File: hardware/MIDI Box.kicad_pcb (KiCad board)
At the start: 2 copper layers, 39.1 x 76.5 mm, 33 parts, among them J1 Conn_01x02_Pin, J2 Conn_01x02_Pin, J3 Conn_01x20_Socket, J4 Conn_01x20_Socket, J7 Conn_01x012_Pin, U1 6N138, U2 6N138, U3 40106

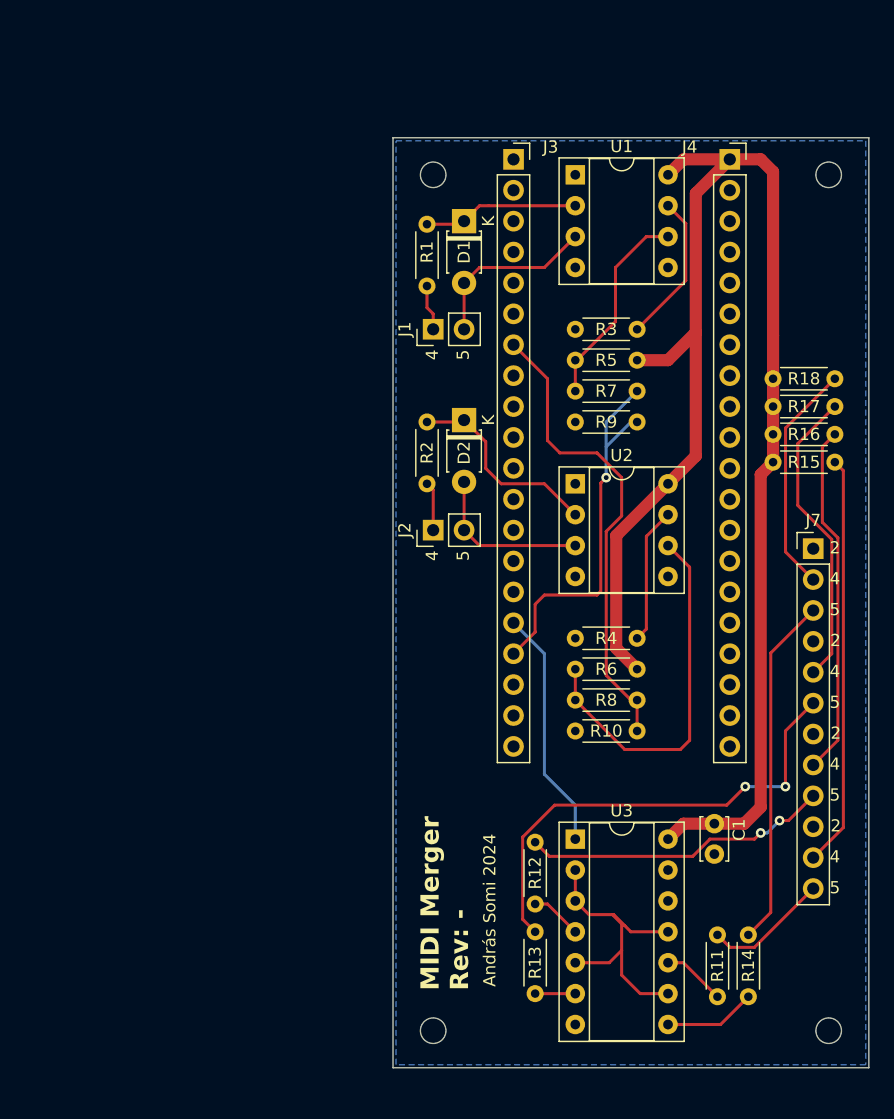
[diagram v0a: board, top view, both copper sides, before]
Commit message: v2.0 board with TRS sockets
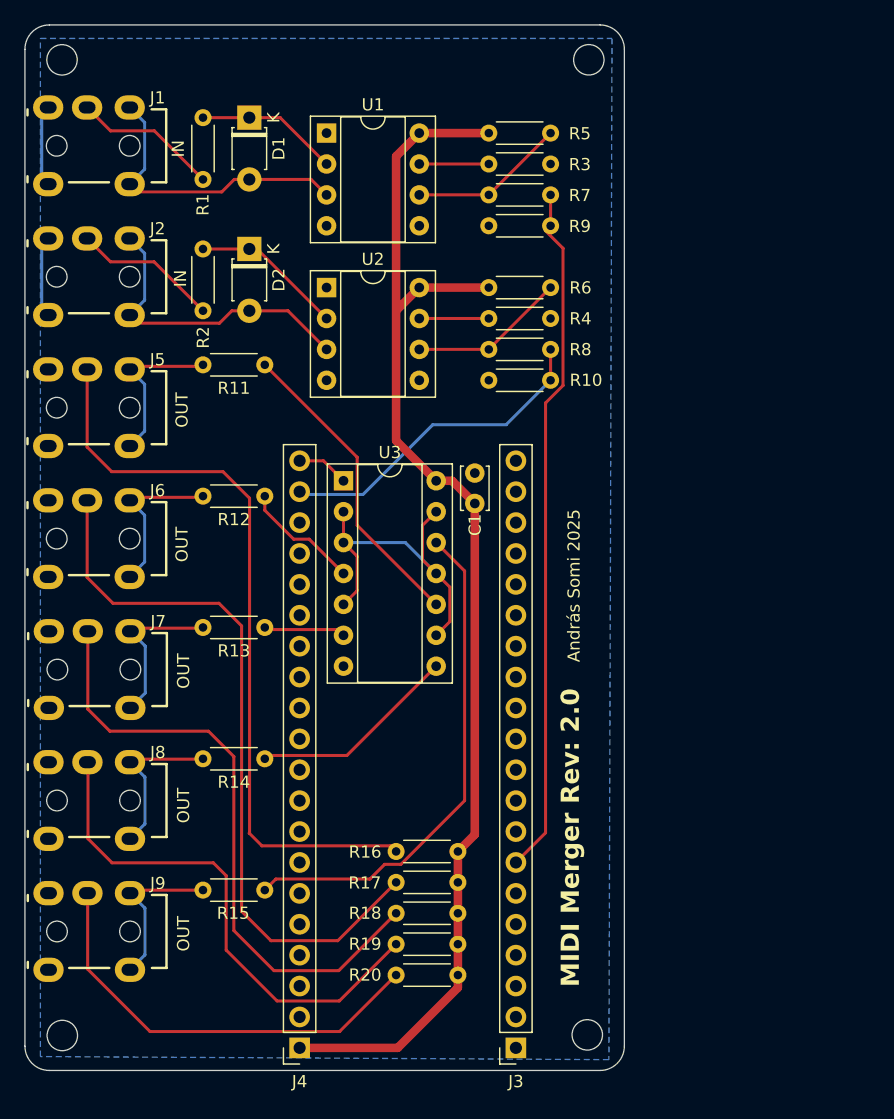
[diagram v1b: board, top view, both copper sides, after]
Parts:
- removed REF** (x4): MountingHole_2.1mm, MountingHole:MountingHole_2.1mm
- added J5: MIDI_OUT_1, own_components:Audio Jack PJ-3136-B, F.Cu at (111.8, 82.9)
- added J6: MIDI_OUT_2, own_components:Audio Jack PJ-3136-B, F.Cu at (111.8, 93.7)
- added J8: MIDI_OUT_4, own_components:Audio Jack PJ-3136-B, F.Cu at (111.9, 115.2)
- added J9: MIDI_OUT_5, own_components:Audio Jack PJ-3136-B, F.Cu at (111.9, 126.0)
- added R19: 220, Resistor_THT:R_Axial_DIN0204_L3.6mm_D1.6mm_P5.08mm_Horizontal, F.Cu at (147.3, 127.0)
- added R20: 220, Resistor_THT:R_Axial_DIN0204_L3.6mm_D1.6mm_P5.08mm_Horizontal, F.Cu at (147.3, 129.5)
- J1: value Conn_01x02_Pin -> MIDI_IN_1; footprint Connector_PinHeader_2.54mm:PinHeader_1x02_P2.54mm_Vertical -> own_components:Audio Jack PJ-3136-B
- J2: value Conn_01x02_Pin -> MIDI_IN_2; footprint Connector_PinHeader_2.54mm:PinHeader_1x02_P2.54mm_Vertical -> own_components:Audio Jack PJ-3136-B
- J7: value Conn_01x012_Pin -> MIDI_OUT_3; footprint Connector_PinHeader_2.54mm:PinHeader_1x12_P2.54mm_Vertical -> own_components:Audio Jack PJ-3136-B
- moved J4 81.1 mm to (134.3, 135.5), turned to 180 degrees
- moved J3 73.0 mm to (152.1, 135.5), turned to 180 degrees
- moved J7 65.4 mm to (111.9, 104.4)
- moved R11 63.9 mm to (131.4, 79.4), turned to 180 degrees
- moved R15 54.6 mm to (131.4, 122.6), turned to 180 degrees
- moved R18 51.0 mm to (147.3, 124.5), turned to 180 degrees
- moved R17 46.9 mm to (147.3, 121.9), turned to 180 degrees
- moved R14 44.3 mm to (131.4, 111.8), turned to 180 degrees
- moved R16 43.0 mm to (147.3, 119.4), turned to 180 degrees
- moved R12 40.2 mm to (131.4, 90.2), turned to 180 degrees
- moved J2 39.4 mm to (111.8, 72.1), turned to 0 degrees
- moved R13 37.4 mm to (131.4, 101.0), turned to 180 degrees
- moved J1 36.7 mm to (111.8, 61.4), turned to 0 degrees
- moved U3 35.1 mm to (137.9, 88.9)
- moved R6 33.7 mm to (149.9, 73.0), turned to 0 degrees
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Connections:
- D1 pad 2: /MIDI_IN1_5 -> Net-(D1-A)
- D2 pad 2: /MIDI_IN2_5 -> Net-(D2-A)
- J3 pad 16: /UART0 TX -> unconnected-(J3-Pin_16-Pad16)
- J3 pad 17: /UART0 RX -> unconnected-(J3-Pin_17-Pad17)
- J4 pad 19: unconnected-(J4-Pin_19-Pad19) -> /UART0 RX
- J4 pad 20: unconnected-(J4-Pin_20-Pad20) -> /UART0 TX
- R1 pad 1: /MIDI_IN1_4 -> Net-(J1-PadR)
- R10 pad 2: /UART1 RX -> /UART0 RX
- R11 pad 2: Net-(J7-Pin_12) -> Net-(J5-PadT)
- R12 pad 2: Net-(J7-Pin_9) -> Net-(J6-PadT)
- R13 pad 2: Net-(J7-Pin_6) -> Net-(J7-PadT)
- R14 pad 2: Net-(J7-Pin_3) -> Net-(J8-PadT)
- R15 pad 1: +5V -> Net-(R15-Pad1)
- R15 pad 2: Net-(J7-Pin_11) -> Net-(J9-PadT)
- R16 pad 2: Net-(J7-Pin_8) -> Net-(J5-PadR)
- R17 pad 2: Net-(J7-Pin_5) -> Net-(J6-PadR)
- R18 pad 2: Net-(J7-Pin_2) -> Net-(J7-PadR)
- R2 pad 1: /MIDI_IN2_4 -> Net-(J2-PadR)
- R7 pad 2: /UART0 RX -> /UART1 RX
- R8 pad 2: /UART1 RX -> /UART0 RX
- R9 pad 2: /UART0 RX -> /UART1 RX
- U1 pad 3: /MIDI_IN1_5 -> Net-(D1-A)
- U2 pad 3: /MIDI_IN2_5 -> Net-(D2-A)
- U3 pad 12: unconnected-(U3-Pad12) -> Net-(R15-Pad1)
- U3 pad 13: GND -> Net-(U3-Pad11)
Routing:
- net Net-(J5-PadR): track 0.00 -> 61.7 mm
- net Net-(J6-PadR): track 0.00 -> 59.8 mm
- net Net-(J7-PadR): track 0.00 -> 51.0 mm
- net Net-(J8-PadR): track 0.00 -> 42.7 mm
- net Net-(R15-Pad1): track 0.00 -> 41.7 mm
- net Net-(J7-Pin_6): track 39.3 -> 0.00 mm, vias 2 -> 0
- net Net-(J9-PadR): track 0.00 -> 35.7 mm
- net Net-(J7-Pin_11): track 33.8 -> 0.00 mm
- net Net-(J7-Pin_8): track 29.0 -> 0.00 mm
- net Net-(J7-Pin_3): track 28.9 -> 0.00 mm
- net Net-(D2-A): track 0.00 -> 26.1 mm
- net Net-(J7-Pin_9): track 25.4 -> 0.00 mm, vias 2 -> 0
- net Net-(D1-A): track 0.00 -> 25.3 mm
- net Net-(J7-Pin_5): track 24.9 -> 0.00 mm
- net Net-(R11-Pad1): track 5.22 -> 25.5 mm
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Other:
- board size 39.1 x 76.5 mm -> 49.3 x 85.9 mm
- board text added: "András Somi 2025"
- board text added: "IN"
- board text added: "MIDI Merger Rev: 2.0"
- board text added: "OUT"
- board text removed: "2"
- board text removed: "4"
- board text removed: "5"
- board text removed: "András Somi 2024"
- board text removed: "MIDI Merger Rev: -"
